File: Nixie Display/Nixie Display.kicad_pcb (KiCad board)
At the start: 2 copper layers, 172.7 x 57.2 mm, 34 parts, among them J1 Conn_01x06_Male, J10 Conn_01x02_Male, J12 Conn_01x02_Male, J2 Conn_01x02_Male, J3 Conn_01x20_Male, J4 Conn_01x02_Male, J5 Conn_01x20_Male, J6 Conn_01x02_Male, J7 Conn_01x20_Male, J8 Conn_01x02_Male, U1 WS2812B, U2 WS2812B, U3 WS2812B, U4 WS2812B, U5 WS2812B, U6 WS2812B

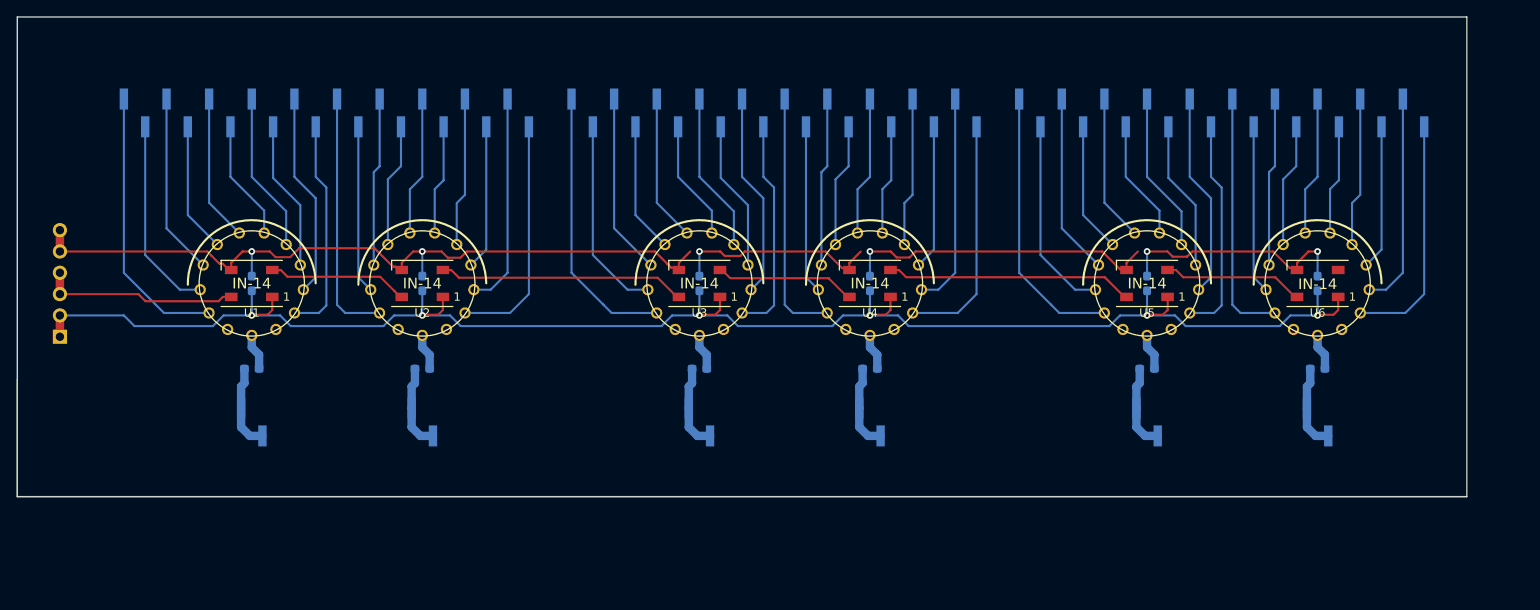
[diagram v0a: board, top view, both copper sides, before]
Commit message: Final V1.0 design. Different sized boards for top and bottom layer. Goal for v2.0 is to have matching top and bottom pcbas
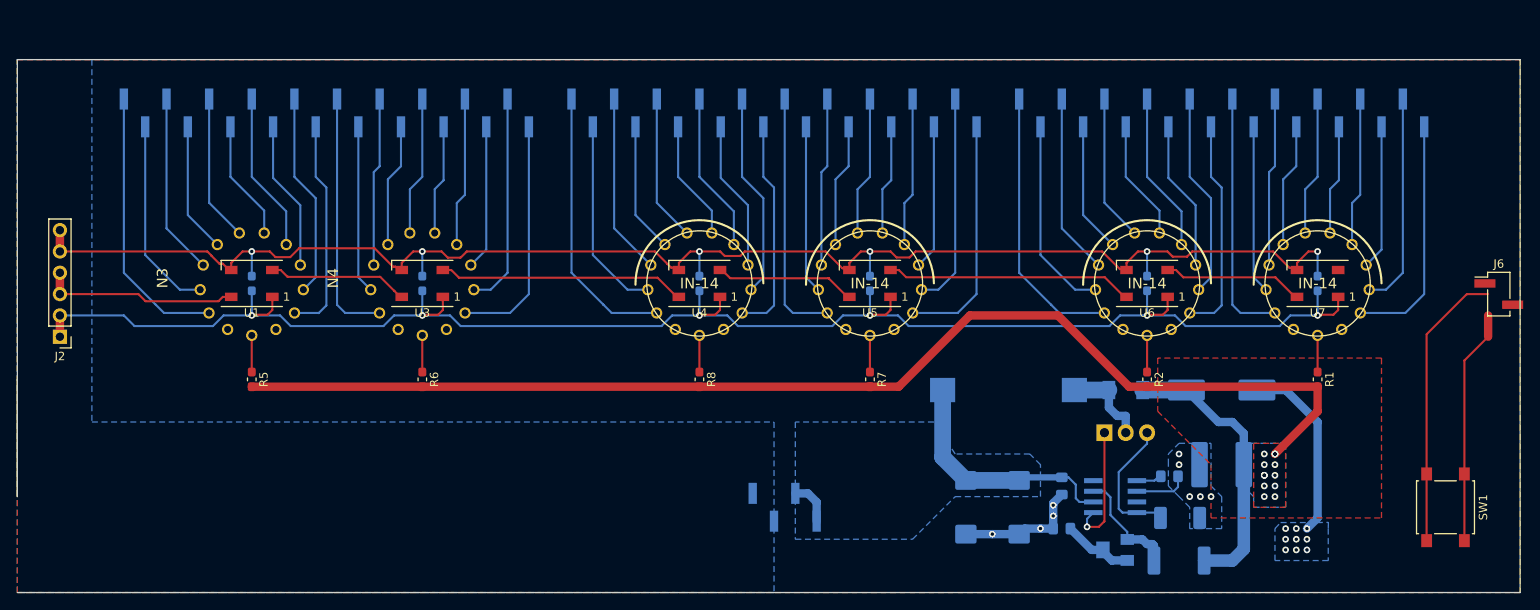
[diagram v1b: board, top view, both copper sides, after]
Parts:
- removed J10, J12, J8: Conn_01x02_Male, Connector_PinHeader_2.54mm:PinHeader_1x02_P2.54mm_Vertical_SMD_Pin1Left
- removed J7: Conn_01x20_Male, Connector_PinHeader_2.54mm:PinHeader_1x20_P2.54mm_Vertical_SMD_Pin1Left
- added C10: 0.1u, Capacitor_SMD:C_0603_1608Metric_Pad1.05x0.95mm_HandSolder, B.Cu at (191.8, 45.7)
- added C11: 0.1u, Capacitor_SMD:C_0603_1608Metric_Pad1.05x0.95mm_HandSolder, B.Cu at (245.1, 45.7)
- added C12: 0.1u, Capacitor_SMD:C_0603_1608Metric_Pad1.05x0.95mm_HandSolder, B.Cu at (224.8, 45.7)
- added C7: 4u7 250V, Capacitor_SMD:CP_Elec_10x14.3, B.Cu at (233.7, 58.4)
- added C8: 100n 250V, Capacitor_SMD:C_2220_5650Metric_Pad1.97x5.40mm_HandSolder, B.Cu at (233.7, 67.3)
- added C9: 0.1u, Capacitor_SMD:C_0603_1608Metric_Pad1.05x0.95mm_HandSolder, B.Cu at (171.4, 45.7)
- added D1: ES2F, Nixie Power and Logic:D_SOD-214AA, B.Cu at (222.2, 58.4)
- added L1: 100uH 1A, Inductor_SMD:L_Bourns_SDR1806, B.Cu at (208.3, 58.4)
- added Q1: IRF644, Package_TO_SOT_THT:TO-220-3_Vertical, B.Cu at (219.7, 63.5)
- added R7: 15k, Resistor_SMD:R_0603_1608Metric_Pad1.05x0.95mm_HandSolder, F.Cu at (191.8, 57.1)
- added R8: 15k, Resistor_SMD:R_0603_1608Metric_Pad1.05x0.95mm_HandSolder, F.Cu at (171.4, 57.1)
- added RSENSE1: 0R050, Resistor_SMD:R_2010_5025Metric_Pad1.52x2.65mm_HandSolder, B.Cu at (228.7, 73.7)
- added RV1: 5k, Potentiometer_SMD:Potentiometer_Bourns_3214W_Vertical, B.Cu at (221.0, 77.5)
- added SW1: SW_Push, Button_Switch_SMD:SW_SPST_B3S-1000, F.Cu at (260.4, 72.4)
- added U7: WS2812B, LED_SMD:LED_WS2812B_PLCC4_5.0x5.0mm_P3.2mm, F.Cu at (245.1, 45.7)
- C1: value 0.1u -> 10uF 25V; footprint Capacitor_SMD:C_0603_1608Metric_Pad1.05x0.95mm_HandSolder -> Capacitor_Tantalum_SMD:CP_EIA-7343-31_Kemet-D_Pad2.25x2.55mm_HandSolder
- C2, C5: value 0.1u -> 100n; footprint Capacitor_SMD:C_0603_1608Metric_Pad1.05x0.95mm_HandSolder -> Capacitor_SMD:C_0805_2012Metric_Pad1.15x1.40mm_HandSolder
- C3: value 0.1u -> 100Uf 35V; footprint Capacitor_SMD:C_0603_1608Metric_Pad1.05x0.95mm_HandSolder -> Capacitor_Tantalum_SMD:CP_EIA-7343-31_Kemet-D_Pad2.25x2.55mm_HandSolder
- J1: value Conn_01x06_Male -> Conn_01x04_Female; footprint Connector_PinHeader_2.54mm:PinHeader_1x06_P2.54mm_Vertical -> Connector_PinHeader_2.54mm:PinHeader_1x04_P2.54mm_Vertical_SMD_Pin1Left
- J2: value Conn_01x02_Male -> Conn_01x06_Male; footprint Connector_PinHeader_2.54mm:PinHeader_1x02_P2.54mm_Vertical_SMD_Pin1Left -> Connector_PinHeader_2.54mm:PinHeader_1x06_P2.54mm_Vertical; moved to F.Cu
- J4: value Conn_01x02_Male -> Conn_01x20_Male; footprint Connector_PinHeader_2.54mm:PinHeader_1x02_P2.54mm_Vertical_SMD_Pin1Left -> Connector_PinHeader_2.54mm:PinHeader_1x20_P2.54mm_Vertical_SMD_Pin1Left
- J6, R1, R2, R5, R6: moved to F.Cu
- N3, N4: moved to B.Cu
- R3: value 15k -> 1M5; footprint Resistor_SMD:R_0603_1608Metric_Pad1.05x0.95mm_HandSolder -> Resistor_SMD:R_2512_6332Metric_Pad1.52x3.35mm_HandSolder
- R4: value 15k -> 10k; footprint Resistor_SMD:R_0603_1608Metric_Pad1.05x0.95mm_HandSolder -> Resistor_SMD:R_0805_2012Metric_Pad1.15x1.40mm_HandSolder
- U2: value WS2812B -> MAX171; footprint LED_SMD:LED_WS2812B_PLCC4_5.0x5.0mm_P3.2mm -> Nixie Power and Logic:SOIC−8-NARROW; moved to B.Cu
- moved J2 150.2 mm to (95.2, 52.1), turned to 180 degrees
- moved J4 104.5 mm to (127.0, 25.4)
- moved C5 91.9 mm to (227.5, 68.7), turned to 0 degrees
- moved J1 88.7 mm to (181.6, 72.4), turned to 90 degrees
- moved U2 86.4 mm to (221.0, 71.1), turned to 90 degrees
- moved J6 76.5 mm to (266.7, 47.0), turned to 0 degrees
- moved N3 73.7 mm to (118.1, 45.7), turned to 180 degrees
- moved N5 53.3 mm to (191.8, 45.7)
- moved C4 53.3 mm to (118.1, 45.7)
- moved N6 53.3 mm to (171.4, 45.7)
- moved C1 49.7 mm to (203.2, 72.4), turned to 270 degrees
- moved R4 47.2 mm to (214.6, 74.9)
- moved R3 43.3 mm to (228.6, 78.7)
- moved N4 33.0 mm to (138.4, 45.7), turned to 180 degrees
- moved U3 33.0 mm to (138.4, 45.7)
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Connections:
- C1 pad 1: +5V -> /vcc
- C2 pad 1: +5V -> /vcc
- C3 pad 1: +5V -> /vcc
- C5 pad 1: +5V -> Net-(C5-Pad1)
- J1 pad 1: +5V -> /vcc
- J1 pad 2: +5V -> /vcc
- J1 pad 3: Net-(J1-Pad3) -> GND
- J1 pad 4: Net-(J1-Pad3) -> GND
- J2 pad 1: Net-(J2-Pad1) -> +5V
- J2 pad 2: Net-(J2-Pad1) -> +5V
- J4 pad 2: Net-(J4-Pad1) -> Net-(J4-Pad2)
- J6 pad 2: Net-(J6-Pad1) -> Net-(J6-Pad2)
- N3 pad 0: Net-(J5-Pad20) -> Net-(J4-Pad20)
- N3 pad 1: Net-(J5-Pad11) -> Net-(J4-Pad11)
- N3 pad 2: Net-(J5-Pad12) -> Net-(J4-Pad12)
- N3 pad 3: Net-(J5-Pad13) -> Net-(J4-Pad13)
- N3 pad 4: Net-(J5-Pad14) -> Net-(J4-Pad14)
- N3 pad 5: Net-(J5-Pad15) -> Net-(J4-Pad15)
- N3 pad 6: Net-(J5-Pad16) -> Net-(J4-Pad16)
- N3 pad 7: Net-(J5-Pad17) -> Net-(J4-Pad17)
- N3 pad 8: Net-(J5-Pad18) -> Net-(J4-Pad18)
- N3 pad 9: Net-(J5-Pad19) -> Net-(J4-Pad19)
- N4 pad 0: Net-(J5-Pad10) -> Net-(J4-Pad10)
- N4 pad 1: Net-(J5-Pad1) -> Net-(J4-Pad1)
- N4 pad 2: Net-(J5-Pad2) -> Net-(J4-Pad2)
- N4 pad 3: Net-(J5-Pad3) -> Net-(J4-Pad3)
- N4 pad 4: Net-(J5-Pad4) -> Net-(J4-Pad4)
- N4 pad 5: Net-(J5-Pad5) -> Net-(J4-Pad5)
- N4 pad 6: Net-(J5-Pad6) -> Net-(J4-Pad6)
- N4 pad 7: Net-(J5-Pad7) -> Net-(J4-Pad7)
- N4 pad 8: Net-(J5-Pad8) -> Net-(J4-Pad8)
- N4 pad 9: Net-(J5-Pad9) -> Net-(J4-Pad9)
- N5 pad 0: Net-(J7-Pad20) -> Net-(J5-Pad20)
- N5 pad 1: Net-(J7-Pad11) -> Net-(J5-Pad11)
- N5 pad 2: Net-(J7-Pad12) -> Net-(J5-Pad12)
- N5 pad 3: Net-(J7-Pad13) -> Net-(J5-Pad13)
- N5 pad 4: Net-(J7-Pad14) -> Net-(J5-Pad14)
- N5 pad 5: Net-(J7-Pad15) -> Net-(J5-Pad15)
- N5 pad 6: Net-(J7-Pad16) -> Net-(J5-Pad16)
- N5 pad 7: Net-(J7-Pad17) -> Net-(J5-Pad17)
- N5 pad 8: Net-(J7-Pad18) -> Net-(J5-Pad18)
- N5 pad 9: Net-(J7-Pad19) -> Net-(J5-Pad19)
- N6 pad 0: Net-(J7-Pad10) -> Net-(J5-Pad10)
- N6 pad 1: Net-(J7-Pad1) -> Net-(J5-Pad1)
- N6 pad 2: Net-(J7-Pad2) -> Net-(J5-Pad2)
- N6 pad 3: Net-(J7-Pad3) -> Net-(J5-Pad3)
- N6 pad 4: Net-(J7-Pad4) -> Net-(J5-Pad4)
- N6 pad 5: Net-(J7-Pad5) -> Net-(J5-Pad5)
- N6 pad 6: Net-(J7-Pad6) -> Net-(J5-Pad6)
- N6 pad 7: Net-(J7-Pad7) -> Net-(J5-Pad7)
- N6 pad 8: Net-(J7-Pad8) -> Net-(J5-Pad8)
- N6 pad 9: Net-(J7-Pad9) -> Net-(J5-Pad9)
- R1 pad 2: Net-(J2-Pad1) -> 180v
- R2 pad 2: Net-(J4-Pad1) -> 180v
- R3 pad 1: Net-(N3-PadA) -> 180v
- R3 pad 2: Net-(J6-Pad1) -> Net-(R3-Pad2)
- R4 pad 1: Net-(N4-PadA) -> Net-(R4-Pad1)
- R4 pad 2: Net-(J8-Pad1) -> GND
- R5 pad 1: Net-(N5-PadA) -> Net-(N3-PadA)
- R5 pad 2: Net-(J10-Pad1) -> 180v
- R6 pad 1: Net-(N6-PadA) -> Net-(N4-PadA)
- R6 pad 2: Net-(J12-Pad1) -> 180v
- U1 pad 4: Net-(J1-Pad3) -> Net-(J2-Pad3)
- U2 pad 1: +5V -> Net-(Q1-Pad1)
- U2 pad 2: Net-(U2-Pad2) -> /vcc
- U2 pad 3: GND -> Net-(R3-Pad2)
- U2 pad 4: Net-(U1-Pad2) -> SHDN
- U3 pad 4: Net-(U2-Pad2) -> Net-(U1-Pad2)
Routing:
- net 180v: track 0.00 -> 177.4 mm, vias 0 -> 12
- net GND: track 183.8 -> 230.6 mm, vias 6 -> 24
- net /vcc: track 0.00 -> 34.7 mm
- net Net-(J7-Pad1): track 32.8 -> 0.00 mm
- net Net-(J4-Pad20): track 0.00 -> 32.8 mm
- net Net-(J7-Pad11): track 30.0 -> 0.00 mm
- net Net-(J4-Pad10): track 0.00 -> 30.0 mm
- net Net-(U2-Pad2): track 29.4 -> 0.00 mm
- net Net-(J7-Pad20): track 28.5 -> 0.00 mm
- net Net-(J6-Pad2): track 0.00 -> 28.0 mm
- net Net-(J7-Pad10): track 26.0 -> 0.00 mm
- net Net-(J4-Pad11): track 0.00 -> 26.0 mm
- net Net-(J7-Pad19): track 25.6 -> 0.00 mm
- net Net-(J4-Pad2): track 0.00 -> 25.6 mm
- net Net-(J7-Pad9): track 24.4 -> 0.00 mm
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- added copper zone on B.Cu, net /vcc
- added copper zone on B.Cu, net 180v
- added copper zone on F.Cu, net 180v
- added copper zone on B.Cu, net GND
- added copper zone on F.Cu, net GND
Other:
- board size 172.7 x 57.2 mm -> 179.1 x 63.5 mm
